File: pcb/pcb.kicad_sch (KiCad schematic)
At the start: 0 parts

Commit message: journal
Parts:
- added U1: ~, symbol VoltLibrary:TL072
- added U2: ~, symbol VoltLibrary:BluetoothTransmitter
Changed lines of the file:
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@@
 	(generator_version "9.0")
 	(paper "A4")
+	(symbol
+		(lib_id "VoltLibrary:BluetoothTransmitter")
+		(at 35.56 72.39 0)
+		(unit 1)
+		(exclude_from_sim no)
+		(in_bom yes)
+		(on_board yes)
+		(dnp no)
+		(fields_autoplaced yes)
+		(property "Reference" "U2"
+			(at 53.34 57.7849 0)
+			(effects
+				(font
+					(size 1.27 1.27)
+				)
+				(justify left)
+			)
+		)
+		(property "Value" "~"
+			(at 53.34 59.69 0)
+			(effects
+				(font
+					(size 1.27 1.27)
+				)
+				(justify left)
+			)
+		)
+		(property "Footprint" ""
+			(at 35.56 72.39 0)
+			(effects
+				(font
+					(size 1.27 1.27)
+				)
+				(hide yes)
+			)
+		)
+		(property "Datasheet" ""
+			(at 35.56 72.39 0)
+			(effects
+				(font
+					(size 1.27 1.27)
+				)
+				(hide yes)
+			)
+		)
+		(property "Description" ""
+			(at 35.56 72.39 0)
+			(effects
+				(font
+					(size 1.27 1.27)
+				)
+				(hide yes)
+			)
+		)
+		(pin "1"
+		)
+		(pin "11"
+		)
+		(pin "9"
+		)
+		(pin "8"
+		)
+		(pin "6"
+		)
+		(pin "7"
+		)
+		(pin "5"
+		)
+		(pin "10"
+		)
+		(pin "4"
+		)
+		(pin "3"
+		)
+		(pin "2"
+		)
+		(instances
+			(project ""
+				(path "/fa437513-580b-4437-95f6-57bf94b875e3"
+					(reference "U2")
+					(unit 1)
+				)
+			)
+		)
+	)
+	(symbol
+		(lib_id "VoltLibrary:TL072")
+		(at 113.03 58.42 0)
+		(mirror y)
+		(unit 1)
+		(exclude_from_sim no)
+		(in_bom yes)
+		(on_board yes)
+		(dnp no)
+		(property "Reference" "U1"
+			(at 113.665 43.18 0)
+			(effects
+				(font
+					(size 1.27 1.27)
+				)
+			)
+		)
+		(property "Value" "~"
+			(at 113.665 45.72 0)
+			(effects
+				(font
+					(size 1.27 1.27)
+				)
+			)
+		)
+		(property "Footprint" ""
+			(at 113.03 58.42 0)
+			(effects
+				(font
+					(size 1.27 1.27)
+				)
+				(hide yes)
+			)
+		)
+		(property "Datasheet" ""
+			(at 113.03 58.42 0)
+			(effects
+				(font
+					(size 1.27 1.27)
+				)
+				(hide yes)
+			)
+		)
+		(property "Description" ""
+			(at 113.03 58.42 0)
+			(effects
+				(font
+					(size 1.27 1.27)
+				)
+				(hide yes)
+			)
+		)
+		(pin "1"
+		)
+		(pin "2"
+		)
+		(pin "3"
+		)
+		(pin "4"
+		)
+		(pin "8"
+		)
+		(pin "7"
+		)
+		(pin "6"
+		)
+		(pin "5"
+		)
+		(instances
+			(project ""
+				(path "/fa437513-580b-4437-95f6-57bf94b875e3"
+					(reference "U1")
+					(unit 1)
+				)
+			)
+		)
+	)
 	(sheet_instances
 		(path "/"

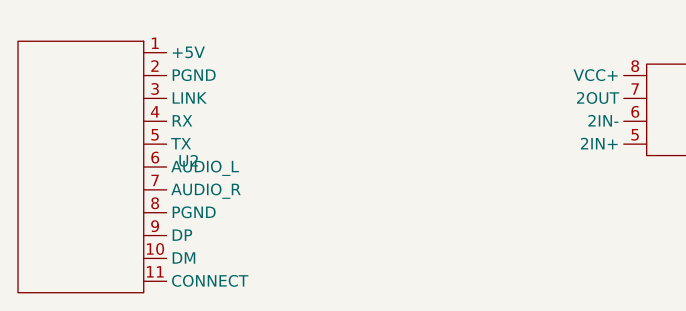
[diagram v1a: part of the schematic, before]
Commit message: fix pin orientation in symbols
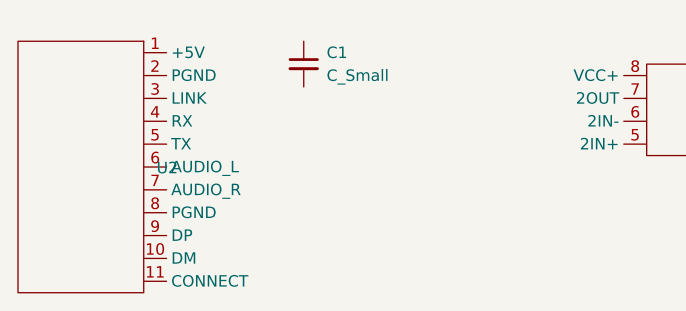
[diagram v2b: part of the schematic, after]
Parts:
- added C1: C_Small, symbol Device:C_Small
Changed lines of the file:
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@@
 		(on_board yes)
 		(dnp no)
-		(fields_autoplaced yes)
 		(property "Reference" "U2"
 			(at 53.34 57.7849 0)
@@
 					(size 1.27 1.27)
 				)
-				(justify left)
+				(justify right top)
 			)
 		)
@@
 					(unit 1)
 				)
+			)
+		)
+	)
+	(symbol
+		(lib_id "Device:C_Small")
+		(at 67.31 46.99 0)
+		(unit 1)
+		(exclude_from_sim no)
+		(in_bom yes)
+		(on_board yes)
+		(dnp no)
+		(fields_autoplaced yes)
+		(property "Reference" "C1"
+			(at 69.85 45.7262 0)
+			(effects
+				(font
+					(size 1.27 1.27)
+				)
+				(justify left)
+			)
+		)
+		(property "Value" "C_Small"
+			(at 69.85 48.2662 0)
+			(effects
+				(font
+					(size 1.27 1.27)
+				)
+				(justify left)
+			)
+		)
+		(property "Footprint" ""
+			(at 67.31 46.99 0)
+			(effects
+				(font
+					(size 1.27 1.27)
+				)
+				(hide yes)
+			)
+		)
+		(property "Datasheet" "~"
+			(at 67.31 46.99 0)
+			(effects
+				(font
+					(size 1.27 1.27)
+				)
+				(hide yes)
+			)
+		)
+		(property "Description" "Unpolarized capacitor, small symbol"
+			(at 67.31 46.99 0)
+			(effects
+				(font
+					(size 1.27 1.27)
+				)
+				(hide yes)
+			)
+		)
+		(pin "1"
+		)
+		(pin "2"
+		)
+		(instances
+			(project ""
+				(path "/fa437513-580b-4437-95f6-57bf94b875e3"
+					(reference "C1")
+					(unit 1)
+				)

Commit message: schematic v1
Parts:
- removed U1: ~, symbol VoltLibrary:TL072
- added C10, C11: 22u, symbol Device:C_Small
- added C12: 10u, symbol Device:C_Small
- added C2: 4u7, symbol Device:C_Small
- added C3, C5, C9: 100n, symbol Device:C_Small
- added C4, C6: 47u, symbol Device:C_Polarized_Small
- added C7: 100u, symbol Device:C_Small
- added C8: 4u7, symbol Device:C_Polarized_Small
- added J1: Conn_01x02, symbol Connector_Generic:Conn_01x02
- added J3: AudioJack2, symbol Connector_Audio:AudioJack2
- added L1: 4u7, symbol Device:L_Small
- added R1: 1M, symbol Device:R_Small
- added R2, R7, R8: 100k, symbol Device:R_Small
- added R3, R4: 10k, symbol Device:R_Small
- added R5: 220k, symbol Device:R_Small
- added R6: 47, symbol Device:R_Small
- added RV1: R_Potentiometer, symbol Device:R_Potentiometer
- added SW1: SW_SPDT, symbol Switch:SW_SPDT
- added U1: TL072, symbol Amplifier_Operational:TL072
- added U3: AP63205WU, Package_TO_SOT_SMD:TSOT-23-6, symbol Regulator_Switching:AP63205WU
- C1: value C_Small -> 1u
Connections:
- net +5V: now reaches U2.1 (+5V)
- net +5V: now also C10.1, C11.1, C7.2, L1.2, U3.1 (FB)
- net GNDPWR: now reaches U2.2 (PGND)
- net GNDPWR: now also U2.8 (AGND), C10.2, C11.2, C12.2, C5.1, C6.2, C7.1, C8.2, J1.2 (Pin_2), J3.S, R8.2, U1.4 (V-), U3.4 (GND)
- net at U2.6 (AUDIO_L): now also U2.7 (AUDIO_R), C8.1, RV1.2
- net GND: now reaches C1.1
- net GND: now also C3.1, C4.2, C5.2, C6.1, J3.T, R2.1, R3.2, R5.2, R6.2, R7.2, R8.1, RV1.1, RV1.3
- net at C1.2: now also R1.1, R2.2
- new net: J1.1 (Pin_1), SW1.2 (B)
- new net: C9.1, L1.1, U3.5 (SW)
- new net: C9.2, U3.6 (BST)
- new net: C2.1, R4.1, U1.1
- new net: R3.1, R4.2, U1.2 (-)
- new net: R1.2, U1.3 (+)
- new net: C2.2, R5.1, R6.1
- new net +9V: C12.1, C3.2, C4.1, R7.1, SW1.3 (C), U1.8 (V+), U3.2 (EN), U3.3 (IN)

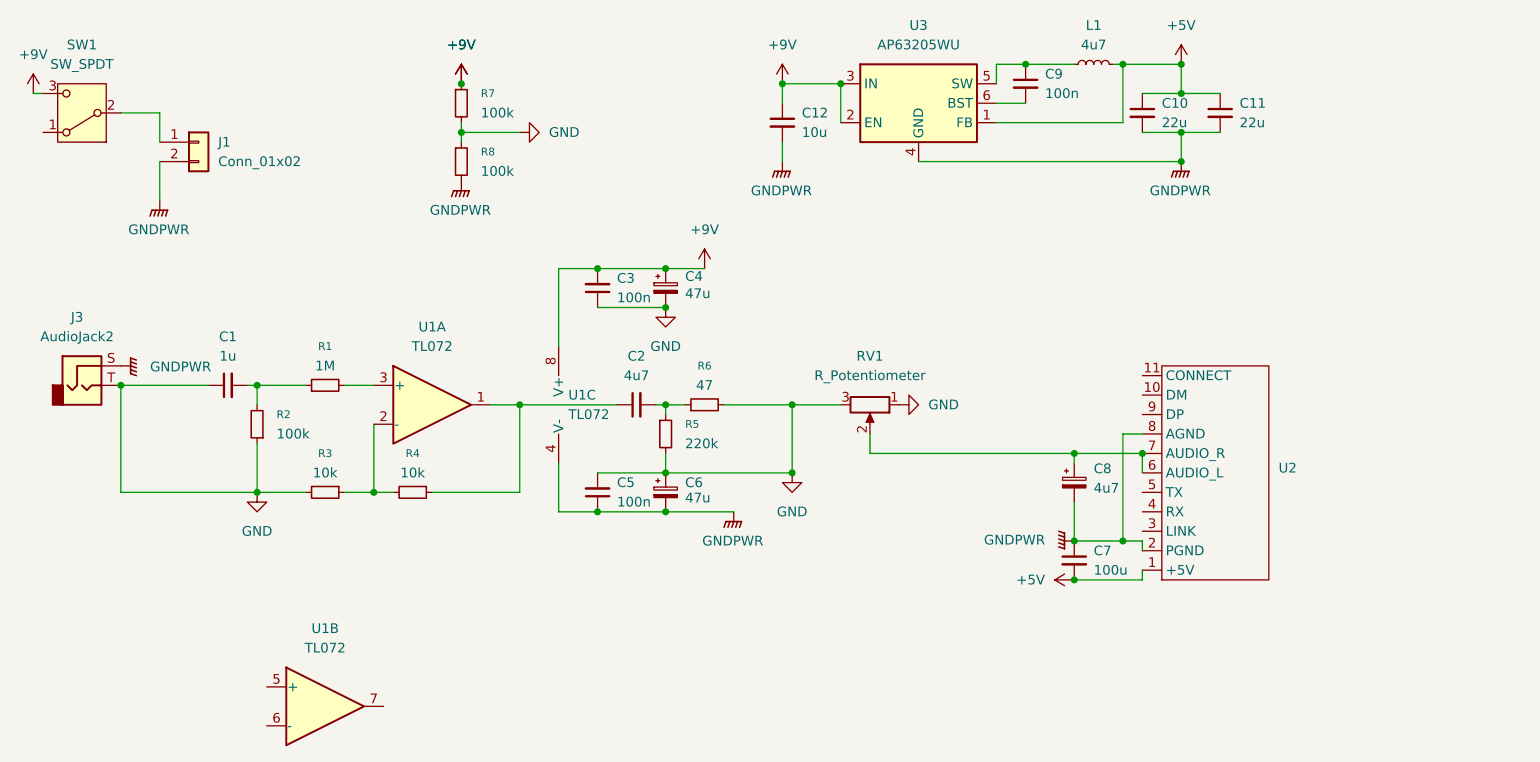
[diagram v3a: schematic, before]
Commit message: small stylistic changes to schematic
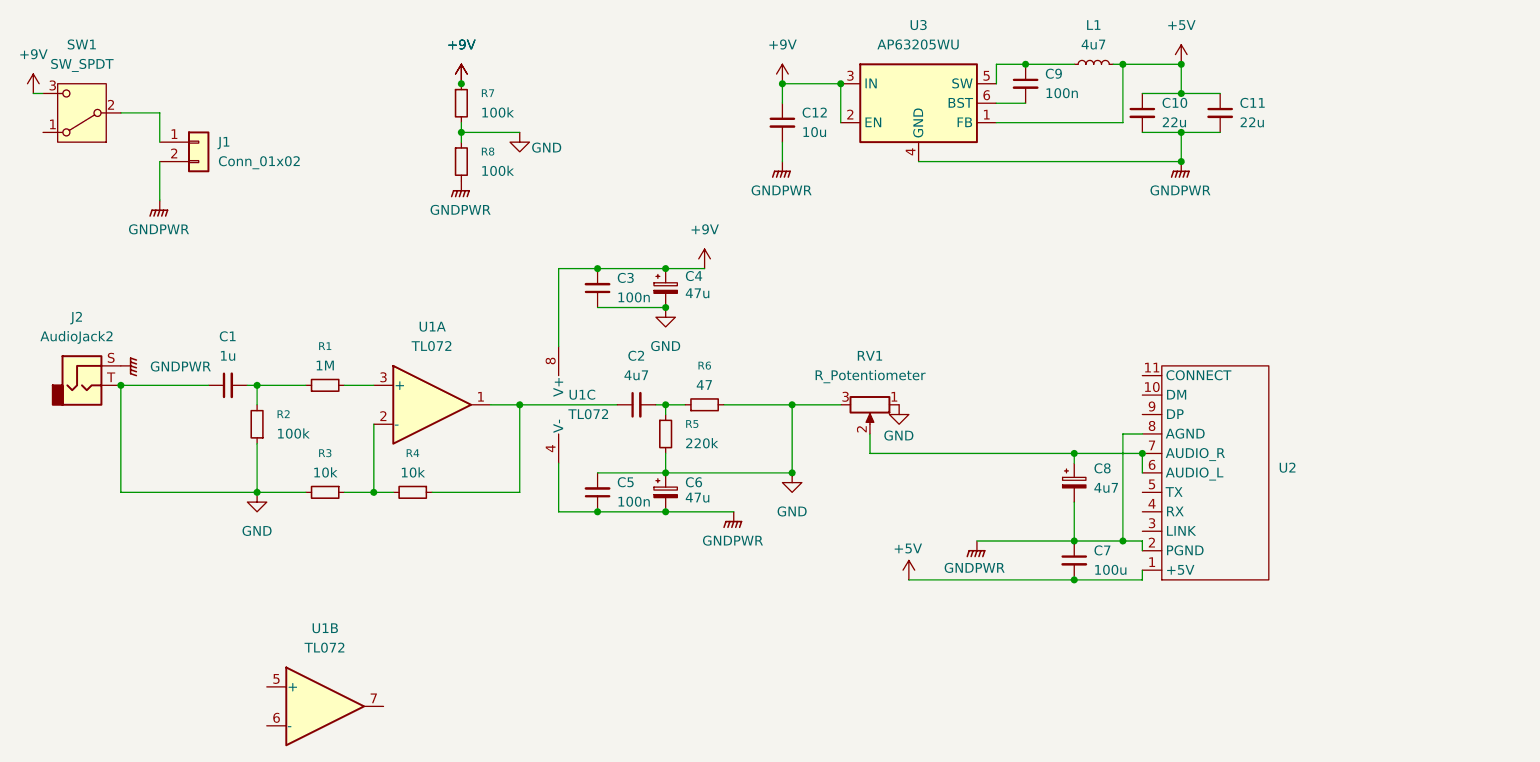
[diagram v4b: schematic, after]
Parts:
- renumbered J3 to J2
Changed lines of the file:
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@@
 	(wire
 		(pts
+			(xy 146.05 86.36) (xy 158.75 86.36)
+		)
+		(stroke
+			(width 0)
+			(type default)
+		)
+	)
+	(wire
+		(pts
 			(xy 120.65 26.67) (xy 120.65 29.21)
 		)
@@
 	(wire
 		(pts
+			(xy 137.16 91.44) (xy 158.75 91.44)
+		)
+		(stroke
+			(width 0)
+			(type default)
+		)
+	)
+	(wire
+		(pts
 			(xy 128.27 26.67) (xy 128.27 31.75)
 		)
@@
 	(symbol
 		(lib_id "power:GNDPWR")
-		(at 158.75 86.36 270)
+		(at 146.05 86.36 0)
 		(unit 1)
 		(exclude_from_sim no)
@@
 		(on_board yes)
 		(dnp no)
-		(fields_autoplaced yes)
 		(property "Reference" "#PWR018"
-			(at 153.67 86.36 0)
+			(at 146.05 91.44 0)
 			(effects
 				(font
@@
 		)
 		(property "Value" "GNDPWR"
-			(at 154.94 86.2329 90)
+			(at 141.732 89.916 0)
 			(effects
 				(font
 					(size 1.27 1.27)
 				)
-				(justify right)
+				(justify left)
 			)
 		)
 		(property "Footprint" ""
-			(at 157.48 86.36 0)
+			(at 146.05 87.63 0)
 			(effects
 				(font
@@
 		)
 		(property "Datasheet" ""
-			(at 157.48 86.36 0)
+			(at 146.05 87.63 0)
 			(effects
 				(font
@@
 		)
 		(property "Description" "Power symbol creates a global label with name \"GNDPWR\" , global ground"
-			(at 158.75 86.36 0)
+			(at 146.05 86.36 0)
 			(effects
 				(font
@@
 		(dnp no)
 		(fields_autoplaced yes)
-		(property "Reference" "J3"
+		(property "Reference" "J2"
 			(at 28.575 57.15 0)
 			(effects
@@
 			(project ""
 				(path "/fa437513-580b-4437-95f6-57bf94b875e3"
-					(reference "J3")
+					(reference "J2")
 					(unit 1)
 				)
@@
 	(symbol
 		(lib_id "power:GND")
-		(at 86.36 33.02 90)
+		(at 86.36 33.02 0)
 		(unit 1)
 		(exclude_from_sim no)
@@
 		(on_board yes)
 		(dnp no)
-		(fields_autoplaced yes)
 		(property "Reference" "#PWR012"
-			(at 92.71 33.02 0)
+			(at 86.36 39.37 0)
 			(effects
 				(font
@@
 		)
 		(property "Value" "GND"
-			(at 90.17 33.0199 90)
+			(at 87.884 35.052 0)
 			(effects
 				(font
 					(size 1.27 1.27)
 				)
-				(justify right)
+				(justify left)
 			)
 		)
@@
 	(symbol
 		(lib_id "power:+5V")
-		(at 158.75 91.44 90)
+		(at 137.16 91.44 0)
 		(unit 1)
 		(exclude_from_sim no)
@@
 		(on_board yes)
 		(dnp no)
-		(fields_autoplaced yes)
 		(property "Reference" "#PWR019"
-			(at 162.56 91.44 0)
+			(at 137.16 95.25 0)
 			(effects
 				(font
@@
 		)
 		(property "Value" "+5V"
-			(at 154.94 91.4399 90)
+			(at 135.128 87.376 0)
 			(effects
 				(font
@@
 		)
 		(property "Footprint" ""
-			(at 158.75 91.44 0)
+			(at 137.16 91.44 0)
 			(effects
 				(font
@@
 		)
 		(property "Datasheet" ""
-			(at 158.75 91.44 0)
+			(at 137.16 91.44 0)
 			(effects
 				(font
@@
 		)
 		(property "Description" "Power symbol creates a global label with name \"+5V\""
-			(at 158.75 91.44 0)
+			(at 137.16 91.44 0)
 			(effects
 				(font
@@
 	(symbol
 		(lib_id "power:GND")
-		(at 135.89 68.58 90)
+		(at 135.89 68.58 0)
 		(unit 1)
 		(exclude_from_sim no)
@@
 		(on_board yes)
 		(dnp no)
-		(fields_autoplaced yes)
 		(property "Reference" "#PWR013"
-			(at 142.24 68.58 0)
+			(at 135.89 74.93 0)
 			(effects
 				(font
@@
 		)
 		(property "Value" "GND"
-			(at 139.7 68.5799 90)
+			(at 133.858 72.644 0)
 			(effects
 				(font
 					(size 1.27 1.27)
 				)
-				(justify right)
+				(justify left)
 			)
 		)

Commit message: footprints, a bit of pcb
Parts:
- removed J2: AudioJack2, symbol Connector_Audio:AudioJack2
- added J2: Conn_01x02, Connector_PinHeader_2.54mm:PinHeader_1x02_P2.54mm_Vertical, symbol Connector_Generic:Conn_01x02
- C1: footprint (none) -> Capacitor_SMD:C_0402_1005Metric; LCSC (none) -> C1525
- C10, C11, C12, C2, C3, C4, C5, C6, C7, C8, C9: footprint (none) -> Capacitor_SMD:C_0402_1005Metric
- J1: footprint (none) -> Connector_PinHeader_2.54mm:PinHeader_1x02_P2.54mm_Vertical
- L1: footprint (none) -> Resistor_SMD:R_0402_1005Metric; LCSC (none) -> C7261423
- R1: footprint (none) -> Resistor_SMD:R_0402_1005Metric; LCSC (none) -> C26083
- R2, R3, R4, R5, R6, R7, R8: footprint (none) -> Resistor_SMD:R_0402_1005Metric
- RV1: footprint (none) -> Connector_PinHeader_2.54mm:PinHeader_1x03_P2.54mm_Vertical
- SW1: footprint (none) -> Button_Switch_SMD:SW_SPDT_PCM12; LCSC (none) -> C221841
- U1: footprint (none) -> TL072CN:DIP254P762X533-8
- U2: footprint (none) -> VoltFootprints:BT_Transmitter
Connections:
- net GND: now also J2.1 (Pin_1)
- net GNDPWR: now also J2.2 (Pin_2)
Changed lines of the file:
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@@
 	)
 	(junction
-		(at 34.29 66.04)
+		(at 158.75 91.44)
 		(diameter 0)
 		(color 0 0 0 0)
 	)
 	(junction
-		(at 158.75 91.44)
+		(at 165.1 86.36)
 		(diameter 0)
 		(color 0 0 0 0)
 	)
 	(junction
-		(at 165.1 86.36)
+		(at 121.92 77.47)
 		(diameter 0)
 		(color 0 0 0 0)
 	)
 	(junction
-		(at 121.92 77.47)
+		(at 34.29 66.04)
 		(diameter 0)
 		(color 0 0 0 0)
@@
 	)
 	(symbol
+		(lib_id "Connector_Generic:Conn_01x02")
+		(at 29.21 66.04 180)
+		(unit 1)
+		(exclude_from_sim no)
+		(in_bom yes)
+		(on_board yes)
+		(dnp no)
+		(fields_autoplaced yes)
+		(property "Reference" "J2"
+			(at 29.21 57.15 0)
+			(effects
+				(font
+					(size 1.27 1.27)
+				)
+			)
+		)
+		(property "Value" "Conn_01x02"
+			(at 29.21 59.69 0)
+			(effects
+				(font
+					(size 1.27 1.27)
+				)
+			)
+		)
+		(property "Footprint" "Connector_PinHeader_2.54mm:PinHeader_1x02_P2.54mm_Vertical"
+			(at 29.21 66.04 0)
+			(effects
+				(font
+					(size 1.27 1.27)
+				)
+				(hide yes)
+			)
+		)
+		(property "Datasheet" "~"
+			(at 29.21 66.04 0)
+			(effects
+				(font
+					(size 1.27 1.27)
+				)
+				(hide yes)
+			)
+		)
+		(property "Description" "Generic connector, single row, 01x02, script generated (kicad-library-utils/schlib/autogen/connector/)"
+			(at 29.21 66.04 0)
+			(effects
+				(font
+					(size 1.27 1.27)
+				)
+				(hide yes)
+			)
+		)
+		(pin "1"
+		)
+		(pin "2"
+		)
+		(instances
+			(project ""
+				(path "/fa437513-580b-4437-95f6-57bf94b875e3"
+					(reference "J2")
+					(unit 1)
+				)
+			)
+		)
+	)
+	(symbol
 		(lib_id "power:+9V")
 		(at 120.65 26.67 0)
@@
 			)
 		)
-		(property "Footprint" ""
+		(property "Footprint" "Connector_PinHeader_2.54mm:PinHeader_1x02_P2.54mm_Vertical"
 			(at 44.45 34.29 0)
 			(effects
@@
 			)
 		)
-		(property "Footprint" ""
+		(property "Footprint" "Resistor_SMD:R_0402_1005Metric"
 			(at 78.74 29.21 0)
 			(effects
@@
 			)
 		)
-		(property "Footprint" ""
+		(property "Footprint" "TL072CN:DIP254P762X533-8"
 			(at 93.98 68.58 0)
 			(effects
@@
 			)
 		)
-		(property "Footprint" ""
+		(property "Footprint" "Resistor_SMD:R_0402_1005Metric"
 			(at 161.29 24.13 0)
 			(effects
@@
 			)
 		)
+		(property "LCSC" "C7261423"
+			(at 161.29 24.13 90)
+			(effects
+				(font
+					(size 1.27 1.27)
+				)
+				(hide yes)
+			)
+		)
 		(pin "1"
 		)
@@
 			)
 		)
-		(property "Footprint" ""
+		(property "Footprint" "Capacitor_SMD:C_0402_1005Metric"
 			(at 158.75 88.9 0)
 			(effects
@@
 			)
 		)
-		(property "Footprint" ""
+		(property "Footprint" "Capacitor_SMD:C_0402_1005Metric"
 			(at 158.75 78.74 0)
 			(effects
@@
 			)
 		)
-		(property "Footprint" ""
+		(property "Footprint" "TL072CN:DIP254P762X533-8"
 			(at 74.93 68.58 0)
 			(effects
@@
 			)
 		)
-		(property "Footprint" ""
+		(property "Footprint" "Capacitor_SMD:C_0402_1005Metric"
 			(at 167.64 30.48 0)
 			(effects
@@
 			)
 		)
-		(property "Footprint" ""
+		(property "Footprint" "TL072CN:DIP254P762X533-8"
 			(at 60.96 107.95 0)
 			(effects
@@
 			)
 		)
-		(property "Footprint" ""
+		(property "Footprint" "Resistor_SMD:R_0402_1005Metric"
 			(at 52.07 71.12 0)
 			(effects
@@
 			)
 		)
-		(property "Footprint" ""
+		(property "Footprint" "Resistor_SMD:R_0402_1005Metric"
 			(at 60.96 80.01 0)
 			(effects
@@
 			)
 		)
-		(property "Footprint" ""
+		(property "Footprint" "Resistor_SMD:R_0402_1005Metric"
 			(at 110.49 68.58 0)
 			(effects
@@
 			)
 		)
-		(property "Footprint" ""
+		(property "Footprint" "Capacitor_SMD:C_0402_1005Metric"
 			(at 96.52 53.34 0)
 			(effects
@@
 			)
 		)
-		(property "Footprint" ""
+		(property "Footprint" "Resistor_SMD:R_0402_1005Metric"
 			(at 105.41 72.39 0)
 			(effects
@@
 			)
 		)
-		(property "Footprint" ""
+		(property "Footprint" "Resistor_SMD:R_0402_1005Metric"
 			(at 60.96 66.04 0)
 			(effects
@@
 			)
 		)
+		(property "LCSC" "C26083"
+			(at 60.96 66.04 90)
+			(effects
+				(font
+					(size 1.27 1.27)
+				)
+				(hide yes)
+			)
+		)
 		(pin "1"
 		)
@@
 			)
 		)
-		(property "Footprint" ""
+		(property "Footprint" "Capacitor_SMD:C_0402_1005Metric"
 			(at 101.6 68.58 0)
 			(effects
@@
 	)
 	(symbol
-		(lib_id "Connector_Audio:AudioJack2")
-		(at 29.21 66.04 0)
-		(unit 1)
-		(exclude_from_sim no)
-		(in_bom yes)
-		(on_board yes)
-		(dnp no)
-		(fields_autoplaced yes)
-		(property "Reference" "J2"
-			(at 28.575 57.15 0)
-			(effects
-				(font
-					(size 1.27 1.27)
-				)
-			)
-		)
-		(property "Value" "AudioJack2"
-			(at 28.575 59.69 0)
-			(effects
-				(font
-					(size 1.27 1.27)
-				)
-			)
-		)
-		(property "Footprint" ""
-			(at 29.21 66.04 0)
-			(effects
-				(font
-					(size 1.27 1.27)
-				)
-				(hide yes)
-			)
-		)
-		(property "Datasheet" "~"
-			(at 29.21 66.04 0)
-			(effects
-				(font
-					(size 1.27 1.27)
-				)
-				(hide yes)
-			)
-		)
-		(property "Description" "Audio Jack, 2 Poles (Mono / TS)"
-			(at 29.21 66.04 0)
-			(effects
-				(font
-					(size 1.27 1.27)
-				)
-				(hide yes)
-			)
-		)
-		(pin "T"
-		)
-		(pin "S"
-		)
-		(instances
-			(project ""
-				(path "/fa437513-580b-4437-95f6-57bf94b875e3"
-					(reference "J2")
-					(unit 1)
-				)
-			)
-		)
-	)
-	(symbol
 		(lib_id "power:+5V")
 		(at 172.72 24.13 0)
@@
 			)
 		)
-		(property "Footprint" ""
+		(property "Footprint" "Capacitor_SMD:C_0402_1005Metric"
 			(at 105.41 53.34 0)
 			(effects
@@
 			)
 		)
-		(property "Footprint" ""
+		(property "Footprint" "Capacitor_SMD:C_0402_1005Metric"
 			(at 152.4 26.67 0)
 			(effects
@@
 			)
 		)
-		(property "Footprint" ""
+		(property "Footprint" "Resistor_SMD:R_0402_1005Metric"
 			(at 78.74 36.83 0)
 			(effects
@@
 			)
 		)
-		(property "Footprint" ""
+		(property "Footprint" "Capacitor_SMD:C_0402_1005Metric"
 			(at 105.41 80.01 0)
 			(effects
@@
 			)
 		)
-		(property "Footprint" ""
+		(property "Footprint" "Capacitor_SMD:C_0402_1005Metric"
 			(at 177.8 30.48 0)
 			(effects
@@
 			)
 		)
-		(property "Footprint" ""
+		(property "Footprint" "VoltFootprints:BT_Transmitter"
 			(at 184.15 63.5 0)
 			(effects
@@
 			)
 		)
-		(property "Footprint" ""
+		(property "Footprint" "Capacitor_SMD:C_0402_1005Metric"
 			(at 120.65 31.75 0)
 			(effects
@@
 			)
 		)
-		(property "Footprint" ""
+		(property "Footprint" "Connector_PinHeader_2.54mm:PinHeader_1x03_P2.54mm_Vertical"
 			(at 132.08 68.58 0)
 			(effects
@@
 			)
 		)
-		(property "Footprint" ""
+		(property "Footprint" "Button_Switch_SMD:SW_SPDT_PCM12"
 			(at 29.21 30.48 0)
 			(effects
@@
 			)
 		)
+		(property "LCSC" "C221841"
+			(at 29.21 30.48 0)
+			(effects
+				(font
+					(size 1.27 1.27)
+				)
+				(hide yes)
+			)
+		)
 		(pin "3"
 		)
@@
 			)
 		)
-		(property "Footprint" ""
+		(property "Footprint" "Capacitor_SMD:C_0402_1005Metric"
 			(at 96.52 80.01 0)
 			(effects
@@
 			)
 		)
-		(property "Footprint" ""
+		(property "Footprint" "Resistor_SMD:R_0402_1005Metric"
 			(at 72.39 80.01 0)
 			(effects
@@
 			)
 		)
-		(property "Footprint" ""
+		(property "Footprint" "Capacitor_SMD:C_0402_1005Metric"
 			(at 48.26 66.04 0)
 			(effects
@@
 			(effects
 				(font
+					(size 1.27 1.27)
+				)
+				(hide yes)
+			)
+		)
+		(property "LCSC" "C1525"
+			(at 48.26 66.04 90)
+			(effects
+				(font
